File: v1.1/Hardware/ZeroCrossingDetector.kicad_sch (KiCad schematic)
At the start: 13 parts, among them Q17 MMBT3904, U12 OPA228

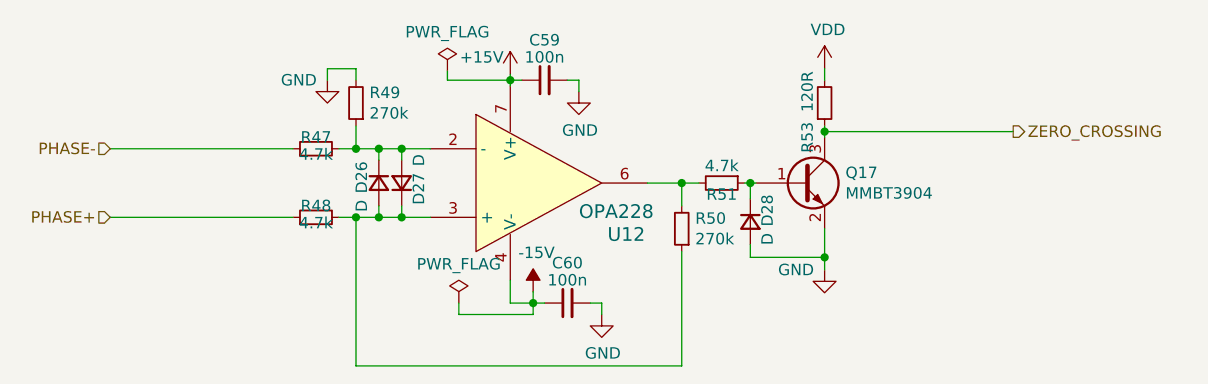
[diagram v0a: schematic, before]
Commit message: v1.1&v1.2 PCB addition.
#####v1.1#####
+Change of MCU; STM32F334C8T6 instead of STM32F103C8T6.
+Filtering 3rd order components of the square wave.
+Use  4 capacitors.
+Adapted to generic transformer(primary 6.4mH, secondary 14.4mH)
+Faster IGBT.

########v1.2#######
+Measures only PZT current and voltage.
+Differential inputs.
+Analog circuitry is capable of measuring four quadrant voltage, current and complex impedance.
+Half bridge configuration.
+Gate resistance of the IGBT's lowered.
+Only USART based touch panel can be connected; not conventional LCD.
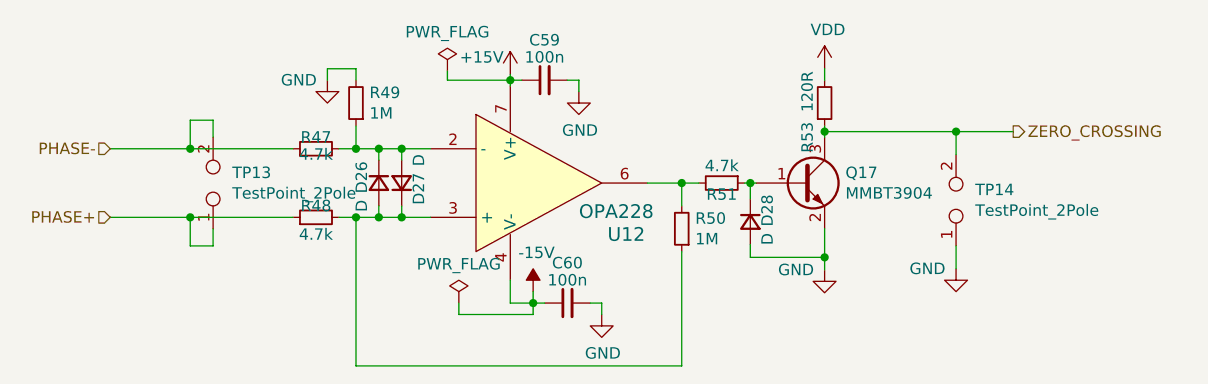
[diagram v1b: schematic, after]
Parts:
- added TP13, TP14: TestPoint_2Pole, Connector_PinHeader_2.54mm:PinHeader_1x02_P2.54mm_Vertical, symbol Connector:TestPoint_2Pole
- C59, C60: footprint Capacitor_SMD:C_0805_2012Metric_Pad1.15x1.40mm_HandSolder -> Capacitor_SMD:C_0805_2012Metric
- R47, R48, R51, R53: footprint Resistor_SMD:R_0805_2012Metric_Pad1.15x1.40mm_HandSolder -> Resistor_SMD:R_0805_2012Metric
- R49, R50: value 270k -> 1M; footprint Resistor_SMD:R_0805_2012Metric_Pad1.15x1.40mm_HandSolder -> Resistor_SMD:R_0805_2012Metric; Link https://ozdisan.com/passive-components/resistors/smt-smd-an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 -> (none); Price 0.01955TL -> 0.01964TL
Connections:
- net GND: now also TP14.1
- net PHASE+: now also TP13.1
- net PHASE-: now also TP13.2
- net ZERO_CROSSING: now also TP14.2
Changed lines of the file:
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@@
 (kicad_sch (version 20200506) (host eeschema "5.99.0-unknown-1f9723c~101~ubuntu18.04.1")
   (page "A4")
+  (junction (at 183.515 81.915))
   (junction (at 121.92 83.82))
-  (junction (at 168.91 81.915))
-  (junction (at 153.035 87.63))
-  (junction (at 136.525 100.965))
-  (junction (at 133.985 76.2))
-  (junction (at 121.92 91.44))
-  (junction (at 119.38 91.44))
-  (junction (at 116.84 83.82))
-  (junction (at 119.38 83.82))
   (junction (at 116.84 91.44))
   (junction (at 168.91 95.885))
+  (junction (at 121.92 91.44))
+  (junction (at 168.91 81.915))
   (junction (at 160.655 87.63))
-  (wire (pts (xy 89.535 83.82) (xy 109.855 83.82)))
-  (wire (pts (xy 89.535 91.44) (xy 109.855 91.44)))
+  (junction (at 119.38 91.44))
+  (junction (at 153.035 87.63))
+  (junction (at 98.425 83.82))
+  (junction (at 119.38 83.82))
+  (junction (at 133.985 76.2))
+  (junction (at 98.425 91.44))
+  (junction (at 116.84 83.82))
+  (junction (at 136.525 100.965))
+  (wire (pts (xy 89.535 83.82) (xy 98.425 83.82)))
+  (wire (pts (xy 89.535 91.44) (xy 98.425 91.44)))
+  (wire (pts (xy 98.425 80.645) (xy 98.425 83.82)))
+  (wire (pts (xy 98.425 83.82) (xy 109.855 83.82)))
+  (wire (pts (xy 98.425 91.44) (xy 109.855 91.44)))
+  (wire (pts (xy 98.425 94.615) (xy 98.425 91.44)))
+  (wire (pts (xy 100.965 80.645) (xy 98.425 80.645)))
+  (wire (pts (xy 100.965 82.55) (xy 100.965 80.645)))
+  (wire (pts (xy 100.965 92.71) (xy 100.965 94.615)))
+  (wire (pts (xy 100.965 94.615) (xy 98.425 94.615)))
   (wire (pts (xy 113.665 74.93) (xy 116.84 74.93)))
   (wire (pts (xy 113.665 76.2) (xy 113.665 74.93)))
@@
   (wire (pts (xy 168.91 81.28) (xy 168.91 81.915)))
   (wire (pts (xy 168.91 81.915) (xy 168.91 82.55)))
-  (wire (pts (xy 168.91 81.915) (xy 189.865 81.915)))
+  (wire (pts (xy 168.91 81.915) (xy 183.515 81.915)))
   (wire (pts (xy 168.91 92.71) (xy 168.91 95.885)))
   (wire (pts (xy 168.91 95.885) (xy 168.91 97.282)))
+  (wire (pts (xy 183.515 81.915) (xy 183.515 84.455)))
+  (wire (pts (xy 183.515 81.915) (xy 189.865 81.915)))
+  (wire (pts (xy 183.515 94.615) (xy 183.515 97.155)))
   (hierarchical_label "PHASE-" (shape input) (at 89.535 83.82 180)
     (effects (font (size 1.27 1.27)) (justify right))
@@
     )
     (property "Datasheet" "" (id 3) (at 168.91 97.282 0)
+      (effects (font (size 1.27 1.27)) hide)
+    )
+  )
+  (symbol (lib_id "power:GND") (at 183.515 97.155 0) (unit 1)
+    (property "Reference" "#PWR0133" (id 0) (at 183.515 103.505 0)
+      (effects (font (size 1.27 1.27)) hide)
+    )
+    (property "Value" "GND" (id 1) (at 180.34 97.155 0))
+    (property "Footprint" "" (id 2) (at 183.515 97.155 0)
+      (effects (font (size 1.27 1.27)) hide)
+    )
+    (property "Datasheet" "" (id 3) (at 183.515 97.155 0)
       (effects (font (size 1.27 1.27)) hide)
     )
@@
     (property "Reference" "R47" (id 0) (at 112.395 82.55 90))
     (property "Value" "4.7k" (id 1) (at 112.395 84.455 90))
-    (property "Footprint" "Resistor_SMD:R_0805_2012Metric_Pad1.15x1.40mm_HandSolder" (id 2) (at 112.395 83.82 0)
+    (property "Footprint" "Resistor_SMD:R_0805_2012Metric" (id 2) (at 112.395 83.82 0)
       (effects (font (size 1.27 1.27)) hide)
     )
@@
   (symbol (lib_id "Device:R_Small") (at 112.395 91.44 90) (unit 1)
     (property "Reference" "R48" (id 0) (at 112.395 90.17 90))
-    (property "Value" "4.7k" (id 1) (at 112.395 92.075 90))
-    (property "Footprint" "Resistor_SMD:R_0805_2012Metric_Pad1.15x1.40mm_HandSolder" (id 2) (at 112.395 91.44 0)
+    (property "Value" "4.7k" (id 1) (at 112.395 93.345 90))
+    (property "Footprint" "Resistor_SMD:R_0805_2012Metric" (id 2) (at 112.395 91.44 0)
       (effects (font (size 1.27 1.27)) hide)
     )
@@
     )
   )
-  (symbol (lib_id "Device:R_Small") (at 116.84 78.74 180) (unit 1)
+  (symbol (lib_name "Device:R_Small_2") (lib_id "Device:R_Small") (at 116.84 78.74 180) (unit 1)
     (property "Reference" "R49" (id 0) (at 118.3386 77.597 0)
       (effects (font (size 1.27 1.27)) (justify right))
     )
-    (property "Value" "270k" (id 1) (at 118.3386 79.883 0)
-      (effects (font (size 1.27 1.27)) (justify right))
-    )
-    (property "Footprint" "Resistor_SMD:R_0805_2012Metric_Pad1.15x1.40mm_HandSolder" (id 2) (at 116.84 78.74 0)
+    (property "Value" "1M" (id 1) (at 118.3386 79.883 0)
+      (effects (font (size 1.27 1.27)) (justify right))
+    )
+    (property "Footprint" "Resistor_SMD:R_0805_2012Metric" (id 2) (at 116.84 78.74 0)
       (effects (font (size 1.27 1.27)) hide)
     )
@@
       (effects (font (size 1.27 1.27)) hide)
     )
-    (property "Link" "https://ozdisan.com/passive-components/resistors/smt-smd-and-chip-resistors/0805S8F2703T5E" (id 4) (at 116.84 78.74 0)
-      (effects (font (size 1.27 1.27)) hide)
-    )
-    (property "Price" "0.01955TL" (id 5) (at 116.84 78.74 0)
-      (effects (font (size 1.27 1.27)) hide)
-    )
-  )
-  (symbol (lib_id "Device:R_Small") (at 153.035 92.71 180) (unit 1)
+    (property "Price" "0.01964TL" (id 4) (at 116.84 78.74 0)
+      (effects (font (size 1.27 1.27)) hide)
+    )
+  )
+  (symbol (lib_name "Device:R_Small_3") (lib_id "Device:R_Small") (at 153.035 92.71 180) (unit 1)
     (property "Reference" "R50" (id 0) (at 154.5336 91.567 0)
       (effects (font (size 1.27 1.27)) (justify right))
     )
-    (property "Value" "270k" (id 1) (at 154.5336 93.853 0)
-      (effects (font (size 1.27 1.27)) (justify right))
-    )
-    (property "Footprint" "Resistor_SMD:R_0805_2012Metric_Pad1.15x1.40mm_HandSolder" (id 2) (at 153.035 92.71 0)
+    (property "Value" "1M" (id 1) (at 154.5336 93.853 0)
+      (effects (font (size 1.27 1.27)) (justify right))
+    )
+    (property "Footprint" "Resistor_SMD:R_0805_2012Metric" (id 2) (at 153.035 92.71 0)
       (effects (font (size 1.27 1.27)) hide)
     )
@@
       (effects (font (size 1.27 1.27)) hide)
     )
-    (property "Link" "https://ozdisan.com/passive-components/resistors/smt-smd-and-chip-resistors/0805S8F2703T5E" (id 4) (at 153.035 92.71 0)
-      (effects (font (size 1.27 1.27)) hide)
-    )
-    (property "Price" "0.01955TL" (id 5) (at 153.035 92.71 0)
+    (property "Price" "0.01964TL" (id 4) (at 153.035 92.71 0)
       (effects (font (size 1.27 1.27)) hide)
     )
@@
     (property "Reference" "R51" (id 0) (at 157.48 88.9 90))
     (property "Value" "4.7k" (id 1) (at 157.48 85.725 90))
-    (property "Footprint" "Resistor_SMD:R_0805_2012Metric_Pad1.15x1.40mm_HandSolder" (id 2) (at 157.48 87.63 0)
+    (property "Footprint" "Resistor_SMD:R_0805_2012Metric" (id 2) (at 157.48 87.63 0)
       (effects (font (size 1.27 1.27)) hide)
     )
@@
     (property "Reference" "R53" (id 0) (at 167.005 82.55 90))
     (property "Value" "120R" (id 1) (at 167.005 77.47 90))
-    (property "Footprint" "Resistor_SMD:R_0805_2012Metric_Pad1.15x1.40mm_HandSolder" (id 2) (at 168.91 78.74 0)
+    (property "Footprint" "Resistor_SMD:R_0805_2012Metric" (id 2) (at 168.91 78.74 0)
       (effects (font (size 1.27 1.27)) hide)
     )
@@
     (property "Reference" "C59" (id 0) (at 137.795 71.755 90))
     (property "Value" "100n" (id 1) (at 137.795 73.66 90))
-    (property "Footprint" "Capacitor_SMD:C_0805_2012Metric_Pad1.15x1.40mm_HandSolder" (id 2) (at 137.795 76.2 0)
+    (property "Footprint" "Capacitor_SMD:C_0805_2012Metric" (id 2) (at 137.795 76.2 0)
       (effects (font (size 1.27 1.27)) hide)
     )
@@
     (property "Reference" "C60" (id 0) (at 140.335 96.52 90))
     (property "Value" "100n" (id 1) (at 140.335 98.425 90))
-    (property "Footprint" "Capacitor_SMD:C_0805_2012Metric_Pad1.15x1.40mm_HandSolder" (id 2) (at 140.335 100.965 0)
+    (property "Footprint" "Capacitor_SMD:C_0805_2012Metric" (id 2) (at 140.335 100.965 0)
       (effects (font (size 1.27 1.27)) hide)
     )
@@
       (effects (font (size 1.27 1.27)) hide)
     )
+  )
+  (symbol (lib_id "Connector:TestPoint_2Pole") (at 100.965 87.63 90) (unit 1)
+    (property "Reference" "TP13" (id 0) (at 103.0986 86.487 90)
+      (effects (font (size 1.27 1.27)) (justify right))
+    )
+    (property "Value" "TestPoint_2Pole" (id 1) (at 103.0986 88.773 90)
+      (effects (font (size 1.27 1.27)) (justify right))
+    )
+    (property "Footprint" "Connector_PinHeader_2.54mm:PinHeader_1x02_P2.54mm_Vertical" (id 2) (at 100.965 87.63 0)
+      (effects (font (size 1.27 1.27)) hide)
+    )
+    (property "Datasheet" "~" (id 3) (at 100.965 87.63 0)
+      (effects (font (size 1.27 1.27)) hide)
+    )
+    (property "Link" "https://ozdisan.com/connectors-and-interconnects/headers/pin-headers/DS1021-1X2SF11-B" (id 4) (at 100.965 87.63 0)
+      (effects (font (size 1.27 1.27)) hide)
+    )
+    (property "Price" "0.08882TL" (id 5) (at 100.965 87.63 0)
+      (effects (font (size 1.27 1.27)) hide)
+    )
+  )
+  (symbol (lib_name "Connector:TestPoint_2Pole_1") (lib_id "Connector:TestPoint_2Pole") (at 183.515 89.535 90) (unit 1)
+    (property "Reference" "TP14" (id 0) (at 185.6487 88.3856 90)
+      (effects (font (size 1.27 1.27)) (justify right))
+    )
+    (property "Value" "TestPoint_2Pole" (id 1) (at 185.6487 90.6843 90)
+      (effects (font (size 1.27 1.27)) (justify right))
+    )
+    (property "Footprint" "Connector_PinHeader_2.54mm:PinHeader_1x02_P2.54mm_Vertical" (id 2) (at 183.515 89.535 0)
+      (effects (font (size 1.27 1.27)) hide)
+    )
+    (property "Datasheet" "~" (id 3) (at 183.515 89.535 0)
+      (effects (font (size 1.27 1.27)) hide)
+    )
+    (property "Link" "https://ozdisan.com/connectors-and-interconnects/headers/pin-headers/DS1021-1X2SF11-B" (id 4) (at 183.515 89.535 0)
+      (effects (font (size 1.27 1.27)) hide)
+    )
+    (property "Price" "0.08882TL" (id 5) (at 183.515 89.535 0)
+      (effects (font (size 1.27 1.27)) hide)
+    )
